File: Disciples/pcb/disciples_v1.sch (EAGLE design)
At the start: 100 parts, among them IC1 OPA1641, IC2 LM324PW, IC3 LM324PW, IC4 TL072D, IC5 LM324PW, IC6 LM4040B10, J1 PJ301_THONKICONN6, J10 PJ301_THONKICONN6, J11 PJ301_THONKICONN6, J2 PJ301_THONKICONN6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

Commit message: Restructure, fixed LEDs
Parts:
- added LED5: WP710A10GD, led:LED3MM
- added R17: 10k, rcl:R-US_R0402
- LED4: value WP-710A10GD -> WP710A10SEC/J3
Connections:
- new net N$46: IC5D.OUT, LED2.A
- new net N$48: IC5D.-IN, LED2.C, R9.1
- net COMP: no longer IC5D.+IN
- net GND: now also R17.2
- net LOWPASS: now also IC5D.+IN
- net N$17: now also LED3.C, R10.2; no longer LED2.C, R9.1
- net N$30: now also LED3.A; no longer LED2.A
- net N$37: now also LED5.C, R17.1; no longer IC5D.-IN, LED3.C, R10.2
- net N$38: now also LED5.A; no longer IC5D.OUT, LED3.A
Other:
- note added: "FWR Clip"
- note added: "Fall"
- note added: "Input Clip"
- note added: "Lowpass/Envelope Level"
- note added: "Rise"
- note added: "Slew Level"
- moved on the sheet: C16, C21, C3, C5, C55, C57, C58, C7, D13, D14, IC1A, IC4A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

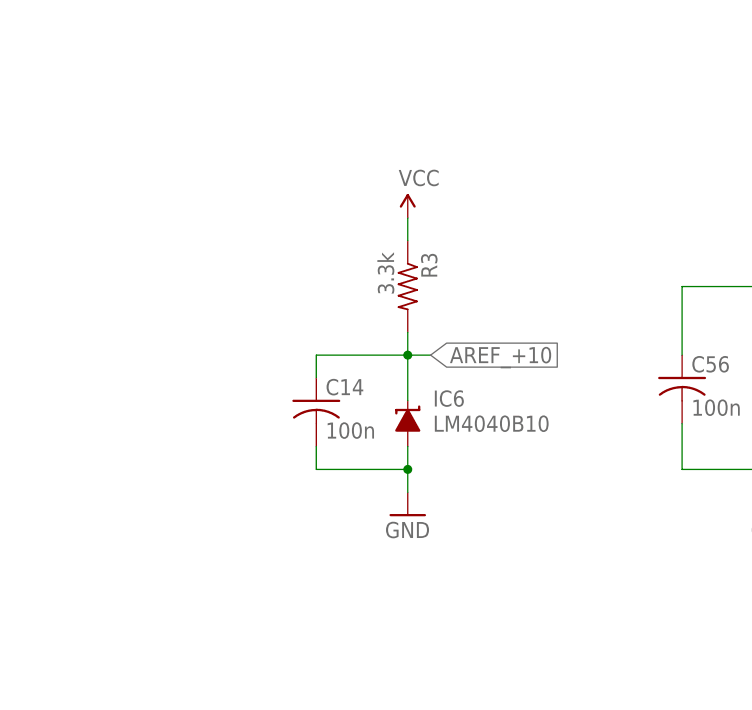
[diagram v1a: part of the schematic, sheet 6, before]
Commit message: More labels, voltage reference
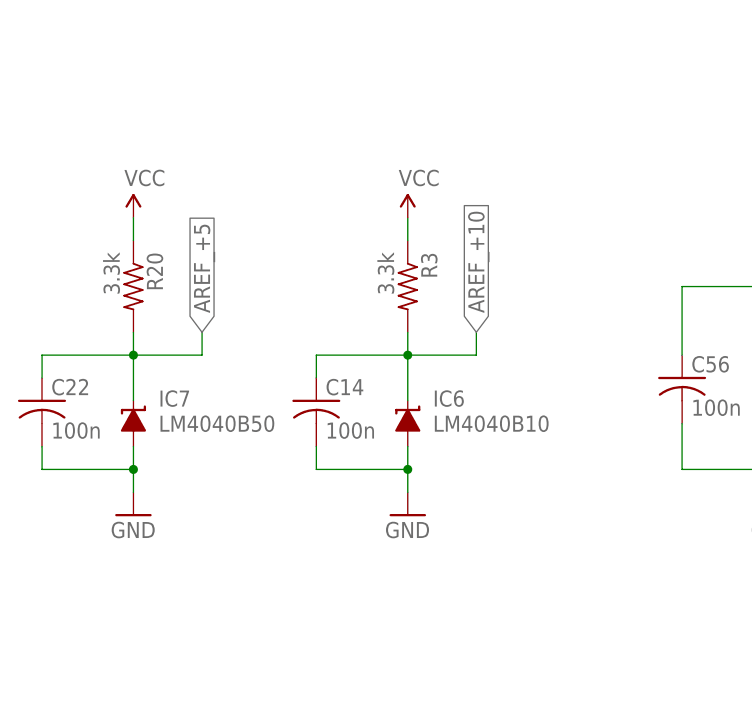
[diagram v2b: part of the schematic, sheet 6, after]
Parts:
- added C22: 100n, rcl:C-USC0603
- added IC7: LM4040B50, texas:LM4041B12DBZ
- added R20: 3.3k, rcl:R-US_R0603
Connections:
- new net AREF_+5: C22.1, IC7.C, R20.2
- net GND: now also C22.2, IC7.A
- net VCC: now also R20.1
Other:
- note added: "Comparator Level"
- note added: "Cutoff Frequency"
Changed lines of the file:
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@@
 <part name="R17" library="rcl" deviceset="R-US_" device="R0402" value="10k"/>
 <part name="LED5" library="led" deviceset="LED" device="3MM" value="WP710A10GD"/>
+<part name="IC7" library="texas" deviceset="LM4041" device="DBZ" technology="B12" value="LM4040B50"/>
+<part name="R20" library="rcl" deviceset="R-US_" device="R0603" value="3.3k"/>
+<part name="C22" library="rcl" deviceset="C-US" device="C0603" value="100n"/>
+<part name="GND31" library="SparkFun" deviceset="GND" device=""/>
+<part name="P+10" library="SparkFun" deviceset="VCC" device=""/>
 </parts>
 <sheets>
@@
 <text x="119.38" y="78.74" size="1.778" layer="91">FIND VAL</text>
 <text x="106.68" y="33.02" size="1.778" layer="97">Lowpass/Envelope Level</text>
+<text x="129.54" y="109.22" size="1.778" layer="97">Cutoff Frequency</text>
 </plain>
 <instances>
@@
 <text x="162.56" y="10.16" size="2.54" layer="94">ellagjameson@gmail.com</text>
 <text x="109.22" y="111.76" size="1.778" layer="91">bipolar op-amp, 0-5v output</text>
+<text x="121.92" y="30.48" size="1.778" layer="97">Comparator Level</text>
 </plain>
 <instances>
@@
 <attribute name="NAME" x="227.076" y="102.235" size="1.778" layer="95"/>
 <attribute name="VALUE" x="227.076" y="97.409" size="1.778" layer="96"/>
+</instance>
+<instance part="IC7" gate="G$1" x="58.42" y="40.64" smashed="yes">
+<attribute name="NAME" x="61.214" y="42.545" size="1.778" layer="95"/>
+<attribute name="VALUE" x="61.214" y="39.751" size="1.778" layer="96"/>
+</instance>
+<instance part="R20" gate="G$1" x="58.42" y="55.88" smashed="yes" rot="R270">
+<attribute name="NAME" x="59.9186" y="59.69" size="1.778" layer="95" rot="R270"/>
+<attribute name="VALUE" x="55.118" y="59.69" size="1.778" layer="96" rot="R270"/>
+</instance>
+<instance part="C22" gate="G$1" x="48.26" y="43.18" smashed="yes">
+<attribute name="NAME" x="49.276" y="43.815" size="1.778" layer="95"/>
+<attribute name="VALUE" x="49.276" y="38.989" size="1.778" layer="96"/>
+</instance>
+<instance part="GND31" gate="1" x="58.42" y="30.48" smashed="yes">
+<attribute name="VALUE" x="55.88" y="27.94" size="1.778" layer="96"/>
+</instance>
+<instance part="P+10" gate="1" x="58.42" y="63.5" smashed="yes">
+<attribute name="VALUE" x="57.404" y="67.056" size="1.778" layer="96"/>
 </instance>
 </instances>
@@
 <pinref part="C20" gate="G$1" pin="1"/>
 </segment>
+<segment>
+<pinref part="GND31" gate="1" pin="GND"/>
+<pinref part="IC7" gate="G$1" pin="A"/>
+<wire x1="58.42" y1="33.02" x2="58.42" y2="35.56" width="0.1524" layer="91"/>
+<pinref part="C22" gate="G$1" pin="2"/>
+<wire x1="58.42" y1="35.56" x2="58.42" y2="38.1" width="0.1524" layer="91"/>
+<wire x1="48.26" y1="38.1" x2="48.26" y2="35.56" width="0.1524" layer="91"/>
+<wire x1="48.26" y1="35.56" x2="58.42" y2="35.56" width="0.1524" layer="91"/>
+<junction x="58.42" y="35.56"/>
+</segment>
 </net>
 <net name="VEE" class="0">
@@
 <pinref part="C19" gate="G$1" pin="1"/>
 </segment>
+<segment>
+<pinref part="R20" gate="G$1" pin="1"/>
+<pinref part="P+10" gate="1" pin="VCC"/>
+<wire x1="58.42" y1="60.96" x2="58.42" y2="63.5" width="0.1524" layer="91"/>
+</segment>
 </net>
 <net name="N$6" class="0">
@@
 <pinref part="R3" gate="G$1" pin="2"/>
 <pinref part="IC6" gate="G$1" pin="C"/>
-<wire x1="91.44" y1="48.26" x2="88.9" y2="48.26" width="0.1524" layer="91"/>
-<label x="91.44" y="48.26" size="1.778" layer="95" xref="yes"/>
+<label x="96.52" y="50.8" size="1.778" layer="95" rot="R90" xref="yes"/>
 <pinref part="C14" gate="G$1" pin="1"/>
 <wire x1="78.74" y1="45.72" x2="78.74" y2="48.26" width="0.1524" layer="91"/>
 <wire x1="78.74" y1="48.26" x2="88.9" y2="48.26" width="0.1524" layer="91"/>
-</segment>
-</net>
+<wire x1="88.9" y1="48.26" x2="96.52" y2="48.26" width="0.1524" layer="91"/>
+<wire x1="96.52" y1="48.26" x2="96.52" y2="50.8" width="0.1524" layer="91"/>
+</segment>
+</net>
+<net name="AREF_+5" class="0">
+<segment>
+<pinref part="IC7" gate="G$1" pin="C"/>
+<pinref part="R20" gate="G$1" pin="2"/>
+<wire x1="58.42" y1="43.18" x2="58.42" y2="48.26" width="0.1524" layer="91"/>
+<pinref part="C22" gate="G$1" pin="1"/>
+<wire x1="58.42" y1="48.26" x2="58.42" y2="50.8" width="0.1524" layer="91"/>
+<wire x1="48.26" y1="45.72" x2="48.26" y2="48.26" width="0.1524" layer="91"/>
+<wire x1="48.26" y1="48.26" x2="58.42" y2="48.26" width="0.1524" layer="91"/>
+<junction x="58.42" y="48.26"/>
+<wire x1="58.42" y1="48.26" x2="66.04" y2="48.26" width="0.1524" layer="91"/>
+<wire x1="66.04" y1="48.26" x2="66.04" y2="50.8" width="0.1524" layer="91"/>
+<label x="66.04" y="50.8" size="1.778" layer="95" rot="R90" xref="yes"/>
+</segment>
+</net>

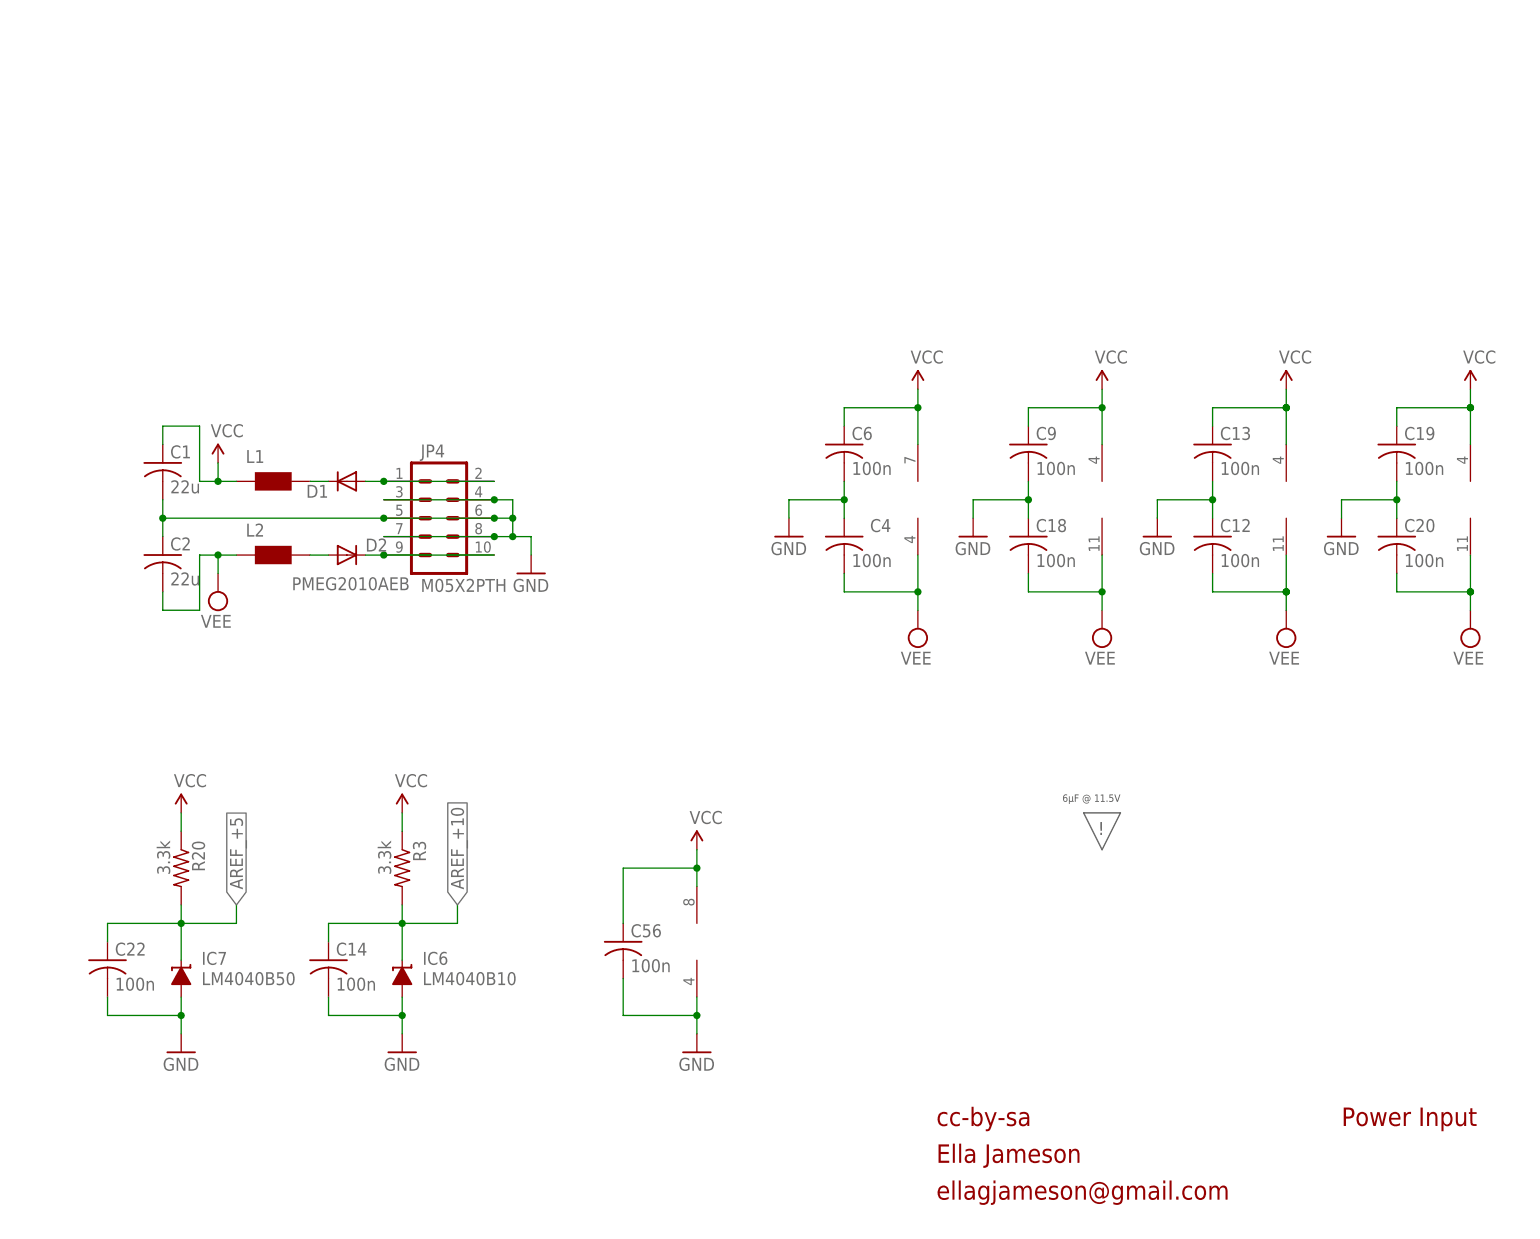
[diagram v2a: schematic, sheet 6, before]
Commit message: Comparator
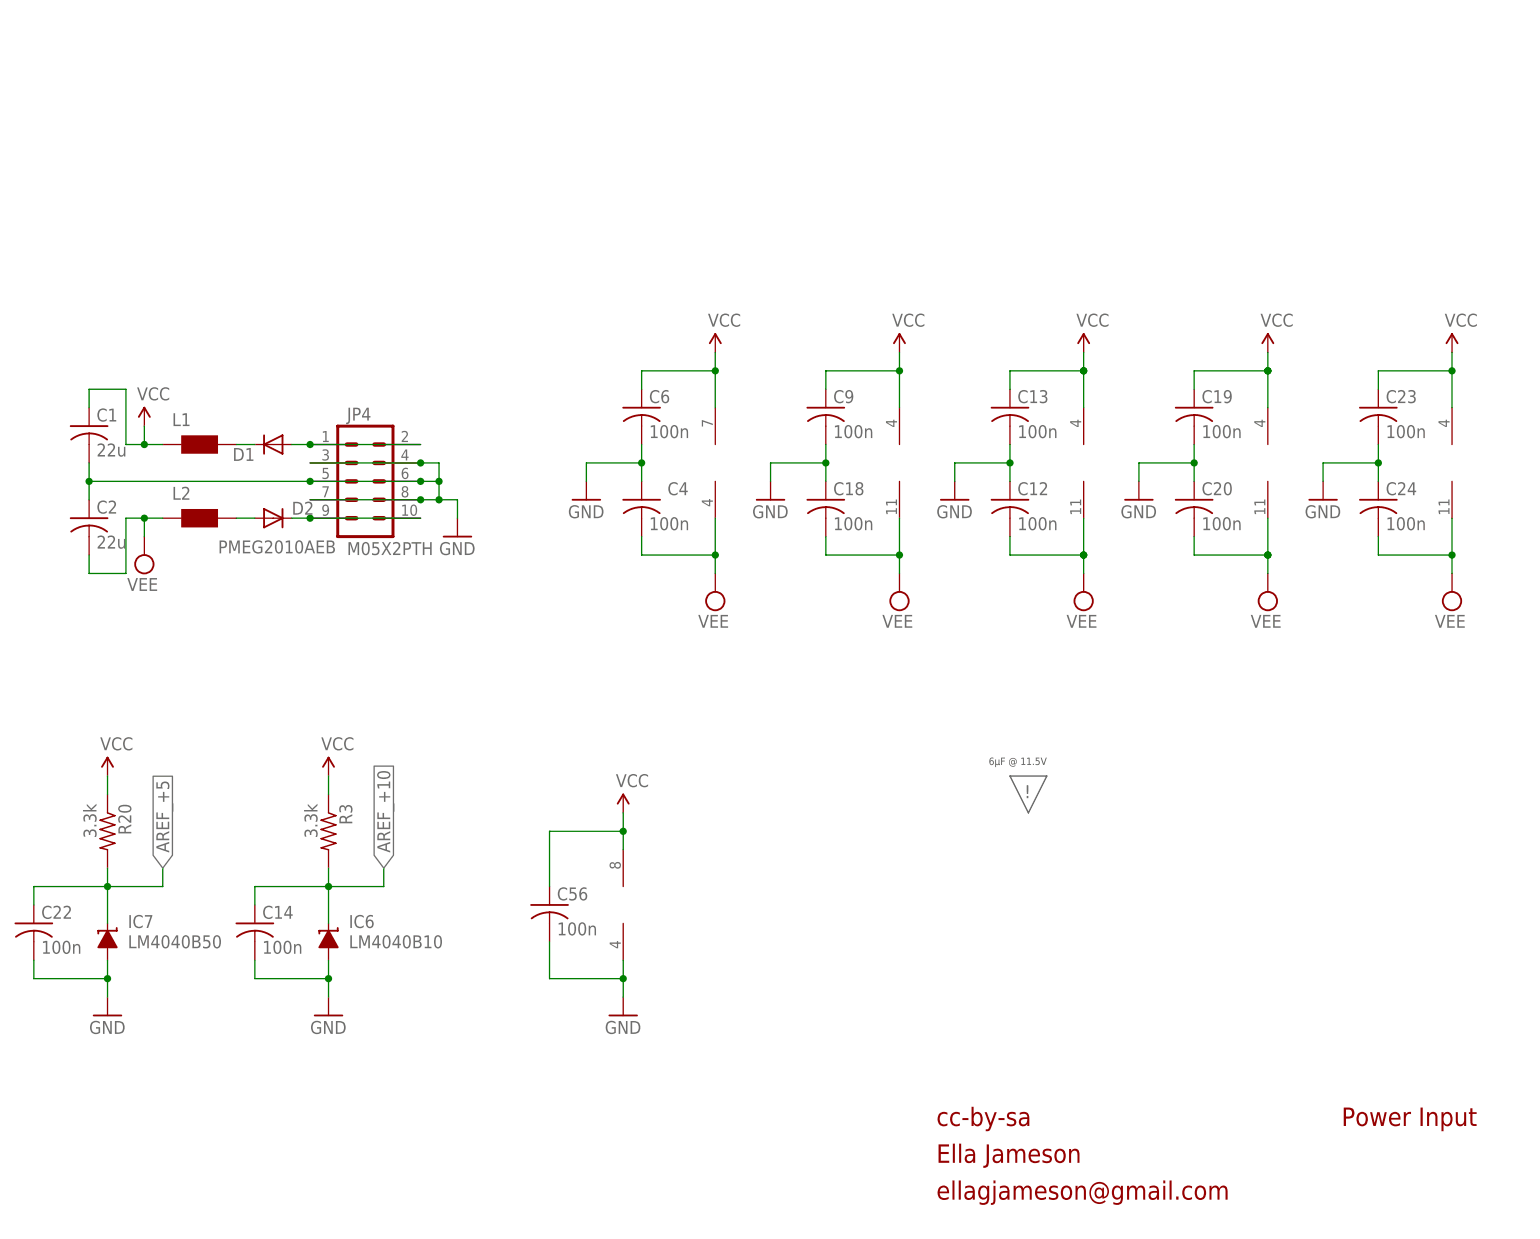
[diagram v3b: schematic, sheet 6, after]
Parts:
- removed C10: 68p, rcl:C-USC0402
- added C23, C24: 100n, rcl:C-USC0402
- added D3, D9: 1N4148, diode:DIODE-SOD523
- added IC8: LM324PW, og-ics:LM324PW
- added R21, R22: 1k, rcl:R-US_R0402
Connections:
- new net COMP_-12_+12: IC8A.OUT, R21.1
- new net N$47: IC8A.+IN, R15.2
- new net N$49: J6.3, R22.1
- new net N$51: D3.C, IC8B.OUT
- new net N$52: D9.A, IC8C.OUT
- net AREF_+5: now also IC8B.+IN
- net COMP: now also D3.A, D9.C, IC8B.-IN, IC8C.-IN, IC8D.+IN, R21.2
- net GND: now also C23.2, C24.1, IC8C.+IN
- net N$27: now also R22.2; no longer J6.3
- net N$37: now also IC8D.-IN
- net N$38: now also IC8D.OUT
- net N$45: now also IC8A.-IN
- net VCC: now also C23.1, IC8P.V+
- net VEE: now also C24.2, IC8P.V-
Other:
- note added: "https://www.analog.com/en/technical-articles/op-amp-precision-positive-negative-clipper-using-lt6015-lt6016-lt6017.html https://everycircuit.com/circuit/5525516952797184"
- note removed: "bipolar op-amp, 0-5v output"
- moved on the sheet: C1, C12, C13, C14, C15, C17, C18, C19, C2, C20, C22, C4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

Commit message: Made schematic
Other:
- note added: "https://www.electroschematics.com/audio-clipping-indicator/"
- moved on the sheet: C16, C3, C5, C7, IC1A, J1, J2, R1, R4, R5, R6, R7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

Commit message: Added slow slew cap (no sw yet)
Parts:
- added C10: 100u, rcl:C-USC0402
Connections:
- net SLEW: now also C10.2
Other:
- note added: "ADD FAST/SLOW SWITCH"
- moved on the sheet: C11
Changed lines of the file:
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@@
 <part name="GND33" library="SparkFun" deviceset="GND" device=""/>
 <part name="R22" library="rcl" deviceset="R-US_" device="R0402" value="1k"/>
+<part name="C10" library="rcl" deviceset="C-US" device="C0402" value="100u"/>
 </parts>
 <sheets>
@@
 <text x="121.92" y="38.1" size="1.778" layer="97">Slew Level</text>
 <text x="180.34" y="99.06" size="1.778" layer="97">Rise</text>
+<text x="180.34" y="132.08" size="1.778" layer="91">ADD FAST/SLOW SWITCH</text>
 </plain>
 <instances>
@@
 <attribute name="VALUE" x="90.17" y="90.678" size="1.778" layer="96"/>
 </instance>
-<instance part="C11" gate="G$1" x="195.58" y="104.14" smashed="yes" rot="R90">
-<attribute name="NAME" x="194.945" y="105.156" size="1.778" layer="95" rot="R90"/>
-<attribute name="VALUE" x="199.771" y="105.156" size="1.778" layer="96" rot="R90"/>
+<instance part="C11" gate="G$1" x="195.58" y="116.84" smashed="yes" rot="R90">
+<attribute name="NAME" x="194.945" y="117.856" size="1.778" layer="95" rot="R90"/>
+<attribute name="VALUE" x="199.771" y="117.856" size="1.778" layer="96" rot="R90"/>
 </instance>
 <instance part="GND6" gate="1" x="101.6" y="83.82" smashed="yes">
@@
 <attribute name="NAME" x="105.41" y="34.5186" size="1.778" layer="95"/>
 <attribute name="VALUE" x="105.41" y="29.718" size="1.778" layer="96"/>
+</instance>
+<instance part="C10" gate="G$1" x="195.58" y="124.46" smashed="yes" rot="R90">
+<attribute name="NAME" x="194.945" y="125.476" size="1.778" layer="95" rot="R90"/>
+<attribute name="VALUE" x="199.771" y="125.476" size="1.778" layer="96" rot="R90"/>
 </instance>
 </instances>
@@
 <segment>
 <wire x1="208.28" y1="93.98" x2="208.28" y2="104.14" width="0.1524" layer="91"/>
-<pinref part="C11" gate="G$1" pin="2"/>
-<wire x1="208.28" y1="104.14" x2="200.66" y2="104.14" width="0.1524" layer="91"/>
 <pinref part="R28" gate="G$1" pin="2"/>
 <wire x1="208.28" y1="104.14" x2="208.28" y2="111.76" width="0.1524" layer="91"/>
@@
 <wire x1="208.28" y1="93.98" x2="205.74" y2="93.98" width="0.1524" layer="91"/>
 <junction x="208.28" y="93.98"/>
+<pinref part="C11" gate="G$1" pin="2"/>
+<wire x1="200.66" y1="116.84" x2="208.28" y2="116.84" width="0.1524" layer="91"/>
+<wire x1="208.28" y1="116.84" x2="208.28" y2="111.76" width="0.1524" layer="91"/>
+<junction x="208.28" y="111.76"/>
+<pinref part="C10" gate="G$1" pin="2"/>
+<wire x1="200.66" y1="124.46" x2="208.28" y2="124.46" width="0.1524" layer="91"/>
+<wire x1="208.28" y1="124.46" x2="208.28" y2="116.84" width="0.1524" layer="91"/>
+<junction x="208.28" y="116.84"/>
 </segment>
 <segment>
@@
 <junction x="177.8" y="96.52"/>
 <wire x1="177.8" y1="96.52" x2="187.96" y2="96.52" width="0.1524" layer="91"/>
-<wire x1="187.96" y1="96.52" x2="187.96" y2="104.14" width="0.1524" layer="91"/>
-<pinref part="C11" gate="G$1" pin="1"/>
-<wire x1="187.96" y1="104.14" x2="193.04" y2="104.14" width="0.1524" layer="91"/>
 <pinref part="IC3" gate="C" pin="-IN"/>
 <wire x1="190.5" y1="96.52" x2="187.96" y2="96.52" width="0.1524" layer="91"/>
 <junction x="187.96" y="96.52"/>
-</segment>
-</net>
+<pinref part="C11" gate="G$1" pin="1"/>
+<wire x1="193.04" y1="116.84" x2="187.96" y2="116.84" width="0.1524" layer="91"/>
+<wire x1="187.96" y1="116.84" x2="187.96" y2="96.52" width="0.1524" layer="91"/>
+</segment>
+</net>

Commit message: CV Pot
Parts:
- added C25, C26: 100n, rcl:C-USC0402
- added IC9: LM324PW, og-ics:LM324PW
- added J12: PJ301_THONKICONN6, og-pj301:PJ301_THONKICONN6
- added R24: 50k, og-pots:POT_USVERTICAL_PS
- added R27: 510, rcl:R-US_R0402
- C21: value TBD -> (none)
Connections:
- new net N$50: IC9A.+IN, R24.S
- new net N$53: J12.3, R27.2
- net AREF_+5: now also R24.A
- net GND: now also C25.2, C26.1, J12.1
- net THRESH: now also IC9A.-IN, IC9A.OUT, R27.1
- net VCC: now also C25.1, IC9P.V+
- net VEE: now also C26.2, IC9P.V-
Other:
- note added: "CV Pot"
